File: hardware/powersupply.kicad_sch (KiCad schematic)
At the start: 17 parts, among them U2 LNK3202D

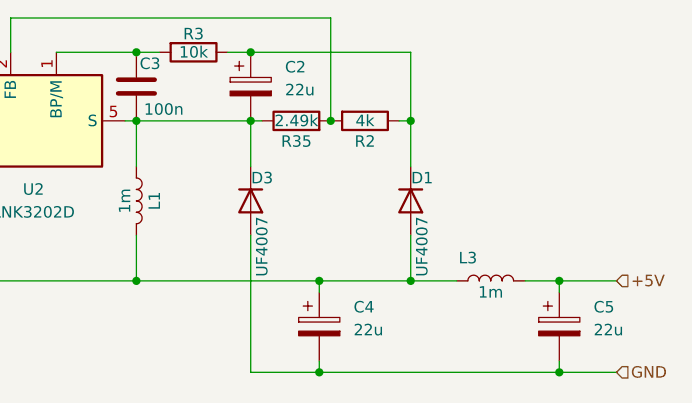
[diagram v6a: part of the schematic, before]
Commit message: added testpoints. adjusted opamps for correct measurement. replaced hard resistors with potentiometer trimmers if necessary
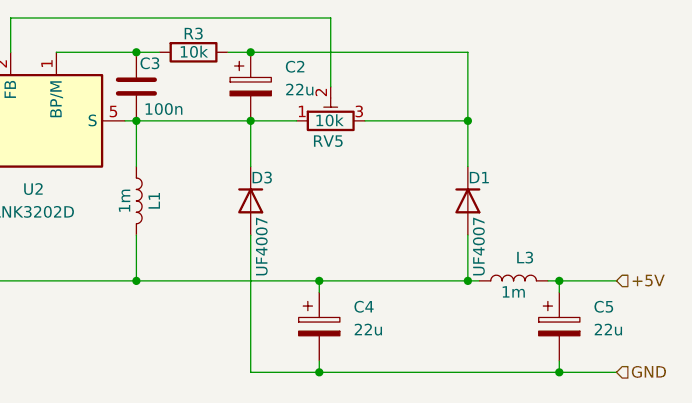
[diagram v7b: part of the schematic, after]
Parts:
- removed R2: 4k, Resistor_SMD:R_0603_1608Metric, symbol Device:R
- removed R35: 2.49k, Resistor_SMD:R_0603_1608Metric, symbol Device:R
- added RV5: 10k, Potentiometer_THT:Potentiometer_Bourns_3299W_Vertical, symbol Device:R_Potentiometer_Trim
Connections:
- net at C2.2, C3.1, D3.1 (K)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: now also RV5.1
- net at U2.2 (FB): now also RV5.2
- net at C2.1, D1.1 (K), R3.1: now also RV5.3
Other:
- moved on the sheet: D1, L3
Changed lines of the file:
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@@
 	(paper "A4")
 	(junction
-		(at 194.31 104.14)
+		(at 200.66 104.14)
+		(diameter 0)
+		(color 0 0 0 0)
+	)
+	(junction
+		(at 200.66 86.36)
 		(diameter 0)
 		(color 0 0 0 0)
@@
 	)
 	(junction
-		(at 194.31 86.36)
-		(diameter 0)
-		(color 0 0 0 0)
-	)
-	(junction
 		(at 163.83 104.14)
 		(diameter 0)
@@
 	)
 	(junction
-		(at 185.42 86.36)
-		(diameter 0)
-		(color 0 0 0 0)
-	)
-	(junction
 		(at 184.15 114.3)
 		(diameter 0)
@@
 	(wire
 		(pts
+			(xy 176.53 78.74) (xy 200.66 78.74)
+		)
+		(stroke
+			(width 0)
+			(type default)
+		)
+	)
+	(wire
+		(pts
 			(xy 210.82 104.14) (xy 210.82 105.41)
 		)
@@
 	(wire
 		(pts
-			(xy 194.31 91.44) (xy 194.31 86.36)
+			(xy 200.66 78.74) (xy 200.66 86.36)
 		)
 		(stroke
@@
 	(wire
 		(pts
-			(xy 194.31 86.36) (xy 194.31 78.74)
-		)
-		(stroke
-			(width 0)
-			(type default)
-		)
-	)
-	(wire
-		(pts
 			(xy 163.83 99.06) (xy 163.83 104.14)
 		)
@@
 	(wire
 		(pts
-			(xy 176.53 78.74) (xy 194.31 78.74)
-		)
-		(stroke
-			(width 0)
-			(type default)
-		)
-	)
-	(wire
-		(pts
-			(xy 194.31 104.14) (xy 199.39 104.14)
+			(xy 200.66 104.14) (xy 201.93 104.14)
 		)
 		(stroke
@@
 	(wire
 		(pts
-			(xy 184.15 104.14) (xy 194.31 104.14)
-		)
-		(stroke
-			(width 0)
-			(type default)
-		)
-	)
-	(wire
-		(pts
-			(xy 194.31 99.06) (xy 194.31 104.14)
+			(xy 200.66 99.06) (xy 200.66 104.14)
 		)
 		(stroke
@@
 	(wire
 		(pts
+			(xy 184.15 104.14) (xy 200.66 104.14)
+		)
+		(stroke
+			(width 0)
+			(type default)
+		)
+	)
+	(wire
+		(pts
 			(xy 125.73 86.36) (xy 125.73 91.44)
 		)
@@
 	(wire
 		(pts
-			(xy 207.01 104.14) (xy 210.82 104.14)
+			(xy 209.55 104.14) (xy 210.82 104.14)
 		)
 		(stroke
@@
 	(wire
 		(pts
-			(xy 193.04 86.36) (xy 194.31 86.36)
-		)
-		(stroke
-			(width 0)
-			(type default)
-		)
-	)
-	(wire
-		(pts
 			(xy 163.83 86.36) (xy 176.53 86.36)
 		)
@@
 	(wire
 		(pts
-			(xy 176.53 86.36) (xy 177.8 86.36)
+			(xy 189.23 86.36) (xy 200.66 86.36)
+		)
+		(stroke
+			(width 0)
+			(type default)
+		)
+	)
+	(wire
+		(pts
+			(xy 176.53 86.36) (xy 181.61 86.36)
 		)
 		(stroke
@@
 	(wire
 		(pts
+			(xy 200.66 86.36) (xy 200.66 91.44)
+		)
+		(stroke
+			(width 0)
+			(type default)
+		)
+	)
+	(wire
+		(pts
 			(xy 173.99 78.74) (xy 176.53 78.74)
 		)
@@
 	(wire
 		(pts
-			(xy 185.42 74.93) (xy 185.42 86.36)
+			(xy 185.42 74.93) (xy 185.42 82.55)
 		)
 		(stroke
@@
 				(path "/ae153005-c1c4-4678-92de-98a47cf88e8d/c42b7df1-fc74-4864-a9e3-b6ebdfdb24fb"
 					(reference "D2")
-					(unit 1)
-				)
-			)
-		)
-	)
-	(symbol
-		(lib_id "Device:R")
-		(at 181.61 86.36 90)
-		(unit 1)
-		(exclude_from_sim no)
-		(in_bom yes)
-		(on_board yes)
-		(dnp no)
-		(property "Reference" "R35"
-			(at 181.61 88.646 90)
-			(effects
-				(font
-					(size 1.27 1.27)
-				)
-			)
-		)
-		(property "Value" "2.49k"
-			(at 181.61 86.36 90)
-			(effects
-				(font
-					(size 1.27 1.27)
-				)
-			)
-		)
-		(property "Footprint" "Resistor_SMD:R_0603_1608Metric"
-			(at 181.61 88.138 90)
-			(effects
-				(font
-					(size 1.27 1.27)
-				)
-				(hide yes)
-			)
-		)
-		(property "Datasheet" "~"
-			(at 181.61 86.36 0)
-			(effects
-				(font
-					(size 1.27 1.27)
-				)
-				(hide yes)
-			)
-		)
-		(property "Description" ""
-			(at 181.61 86.36 0)
-			(effects
-				(font
-					(size 1.27 1.27)
-				)
-				(hide yes)
-			)
-		)
-		(pin "1"
-		)
-		(pin "2"
-		)
-		(instances
-			(project "Steuerplatine"
-				(path "/ae153005-c1c4-4678-92de-98a47cf88e8d/c42b7df1-fc74-4864-a9e3-b6ebdfdb24fb"
-					(reference "R35")
-					(unit 1)
-				)
-			)
-		)
-	)
-	(symbol
-		(lib_id "Device:R")
-		(at 189.23 86.36 270)
-		(unit 1)
-		(exclude_from_sim no)
-		(in_bom yes)
-		(on_board yes)
-		(dnp no)
-		(property "Reference" "R2"
-			(at 189.23 88.646 90)
-			(effects
-				(font
-					(size 1.27 1.27)
-				)
-			)
-		)
-		(property "Value" "4k"
-			(at 189.23 86.36 90)
-			(effects
-				(font
-					(size 1.27 1.27)
-				)
-			)
-		)
-		(property "Footprint" "Resistor_SMD:R_0603_1608Metric"
-			(at 189.23 84.582 90)
-			(effects
-				(font
-					(size 1.27 1.27)
-				)
-				(hide yes)
-			)
-		)
-		(property "Datasheet" "~"
-			(at 189.23 86.36 0)
-			(effects
-				(font
-					(size 1.27 1.27)
-				)
-				(hide yes)
-			)
-		)
-		(property "Description" ""
-			(at 189.23 86.36 0)
-			(effects
-				(font
-					(size 1.27 1.27)
-				)
-				(hide yes)
-			)
-		)
-		(pin "1"
-		)
-		(pin "2"
-		)
-		(instances
-			(project "Steuerplatine"
-				(path "/ae153005-c1c4-4678-92de-98a47cf88e8d/c42b7df1-fc74-4864-a9e3-b6ebdfdb24fb"
-					(reference "R2")
 					(unit 1)
 				)
@@
 	)
 	(symbol
+		(lib_id "Device:R_Potentiometer_Trim")
+		(at 185.42 86.36 90)
+		(unit 1)
+		(exclude_from_sim no)
+		(in_bom yes)
+		(on_board yes)
+		(dnp no)
+		(property "Reference" "RV5"
+			(at 183.388 88.646 90)
+			(effects
+				(font
+					(size 1.27 1.27)
+				)
+				(justify right)
+			)
+		)
+		(property "Value" "10k"
+			(at 183.642 86.36 90)
+			(effects
+				(font
+					(size 1.27 1.27)
+				)
+				(justify right)
+			)
+		)
+		(property "Footprint" "Potentiometer_THT:Potentiometer_Bourns_3299W_Vertical"
+			(at 185.42 86.36 0)
+			(effects
+				(font
+					(size 1.27 1.27)
+				)
+				(hide yes)
+			)
+		)
+		(property "Datasheet" "~"
+			(at 185.42 86.36 0)
+			(effects
+				(font
+					(size 1.27 1.27)
+				)
+				(hide yes)
+			)
+		)
+		(property "Description" "Trim-potentiometer"
+			(at 185.42 86.36 0)
+			(effects
+				(font
+					(size 1.27 1.27)
+				)
+				(hide yes)
+			)
+		)
+		(pin "3"
+		)
+		(pin "2"
+		)
+		(pin "1"
+		)
+		(instances
+			(project "Steuerplatine"
+				(path "/ae153005-c1c4-4678-92de-98a47cf88e8d/c42b7df1-fc74-4864-a9e3-b6ebdfdb24fb"
+					(reference "RV5")
+					(unit 1)
+				)
+			)
+		)
+	)
+	(symbol
 		(lib_id "Regulator_Switching:LNK3202D")
 		(at 152.4 86.36 0)
@@
 	(symbol
 		(lib_id "Device:D")
-		(at 194.31 95.25 270)
+		(at 200.66 95.25 270)
 		(unit 1)
 		(exclude_from_sim no)
@@
 		(dnp no)
 		(property "Reference" "D1"
-			(at 195.58 92.71 90)
+			(at 201.93 92.71 90)
 			(effects
 				(font
@@
 		)
 		(property "Value" "UF4007"
-			(at 195.58 100.33 0)
+			(at 201.93 100.33 0)
 			(effects
 				(font
@@
 		)
 		(property "Footprint" "Diode_SMD:D_SMB"
-			(at 194.31 95.25 0)
+			(at 200.66 95.25 0)
 			(effects
 				(font
@@
 		)
 		(property "Datasheet" "~"
-			(at 194.31 95.25 0)
+			(at 200.66 95.25 0)
 			(effects
 				(font
@@
 		)
 		(property "Description" ""
-			(at 194.31 95.25 0)
+			(at 200.66 95.25 0)
 			(effects
 				(font
@@
 	(symbol
 		(lib_id "Device:L")
-		(at 203.2 104.14 90)
+		(at 205.74 104.14 90)
 		(unit 1)
 		(exclude_from_sim no)
@@
 		(dnp no)
 		(property "Reference" "L3"
-			(at 200.66 101.6 90)
+			(at 207.01 101.6 90)
 			(effects
 				(font
@@
 		)
 		(property "Value" "1m"
-			(at 203.2 105.41 90)
+			(at 205.74 105.41 90)
 			(effects
 				(font
@@
 		)
 		(property "Footprint" "Inductor_SMD:L_Wuerth_WE-XHMI-8080"
-			(at 203.2 104.14 0)
+			(at 205.74 104.14 0)
 			(effects
 				(font
@@
 		)
 		(property "Datasheet" "~"
-			(at 203.2 104.14 0)
+			(at 205.74 104.14 0)
 			(effects
 				(font
@@
 		)
 		(property "Description" ""
-			(at 203.2 104.14 0)
-			(effects
-				(font
+			(at 205.74 104.14 0)
+			(effects
+				(font
